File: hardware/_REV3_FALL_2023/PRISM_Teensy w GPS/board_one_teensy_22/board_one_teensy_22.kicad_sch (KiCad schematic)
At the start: 30 parts, among them J1 Micro_SD_Card_Det_Hirose_DM3AT, J3 3387, Q1 AO3400A, Q2 AO3400A, U1 Teensy4.0, U2 GPS-14414, U3 3966, U4 RFM69HCW_Breakout, U5 CT25E-16T150-1, U6 CMI-9605-1280T

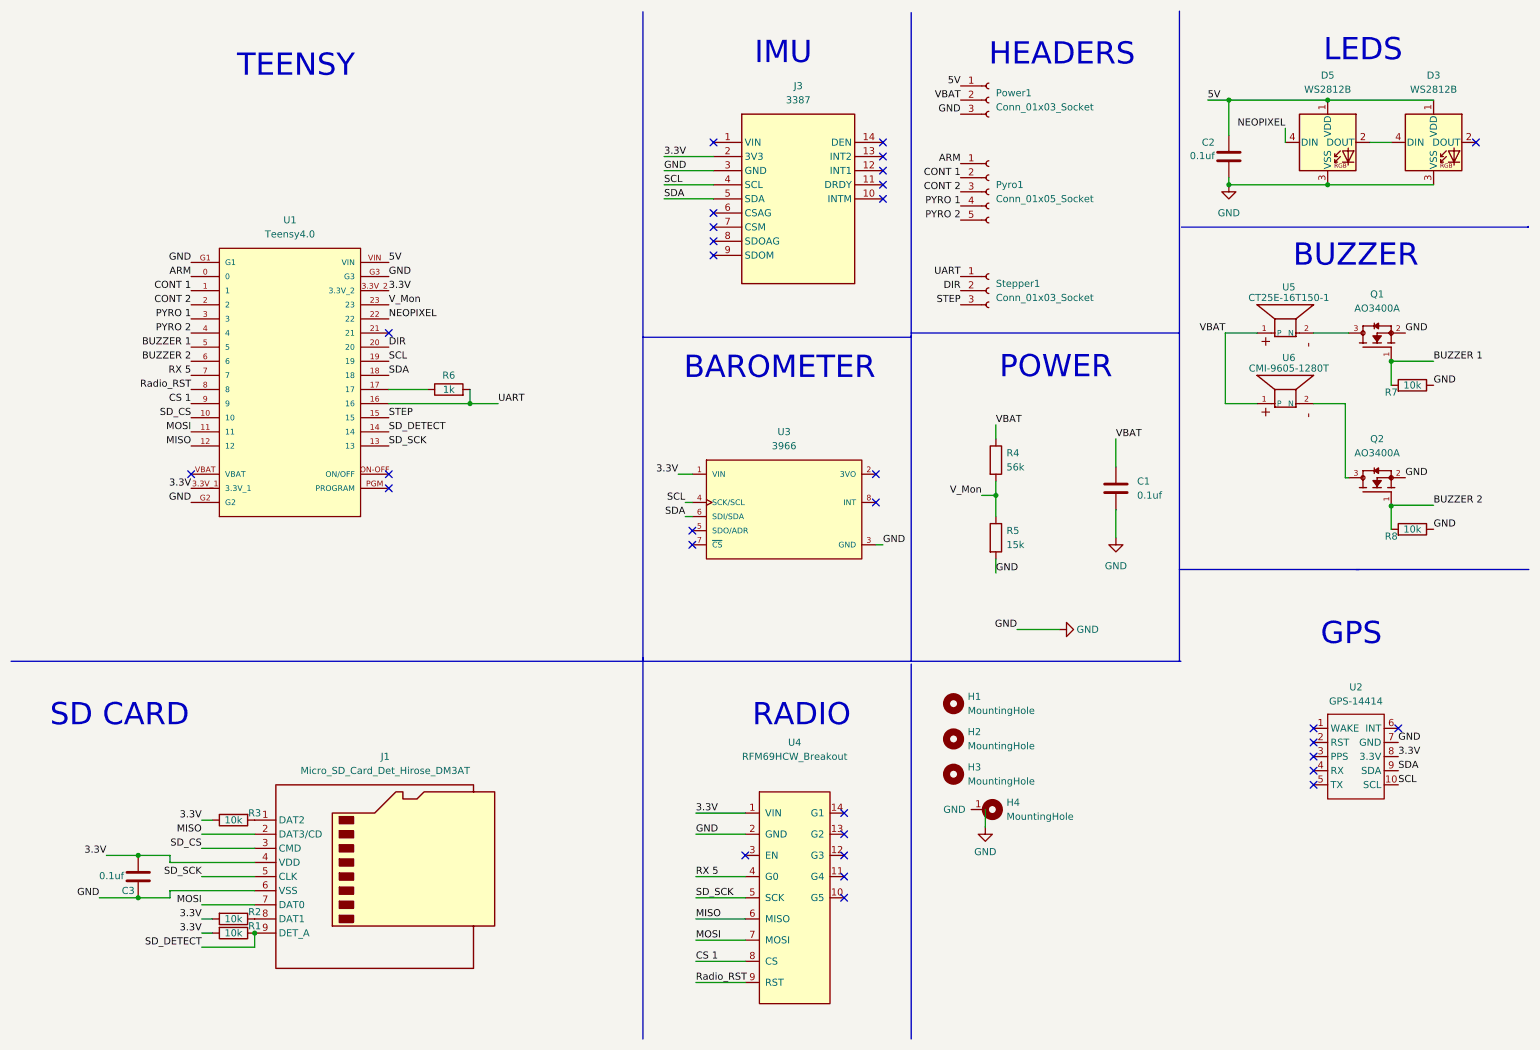
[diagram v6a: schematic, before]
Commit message: Added 3.3V line and fixed analog routing issues on Teensy
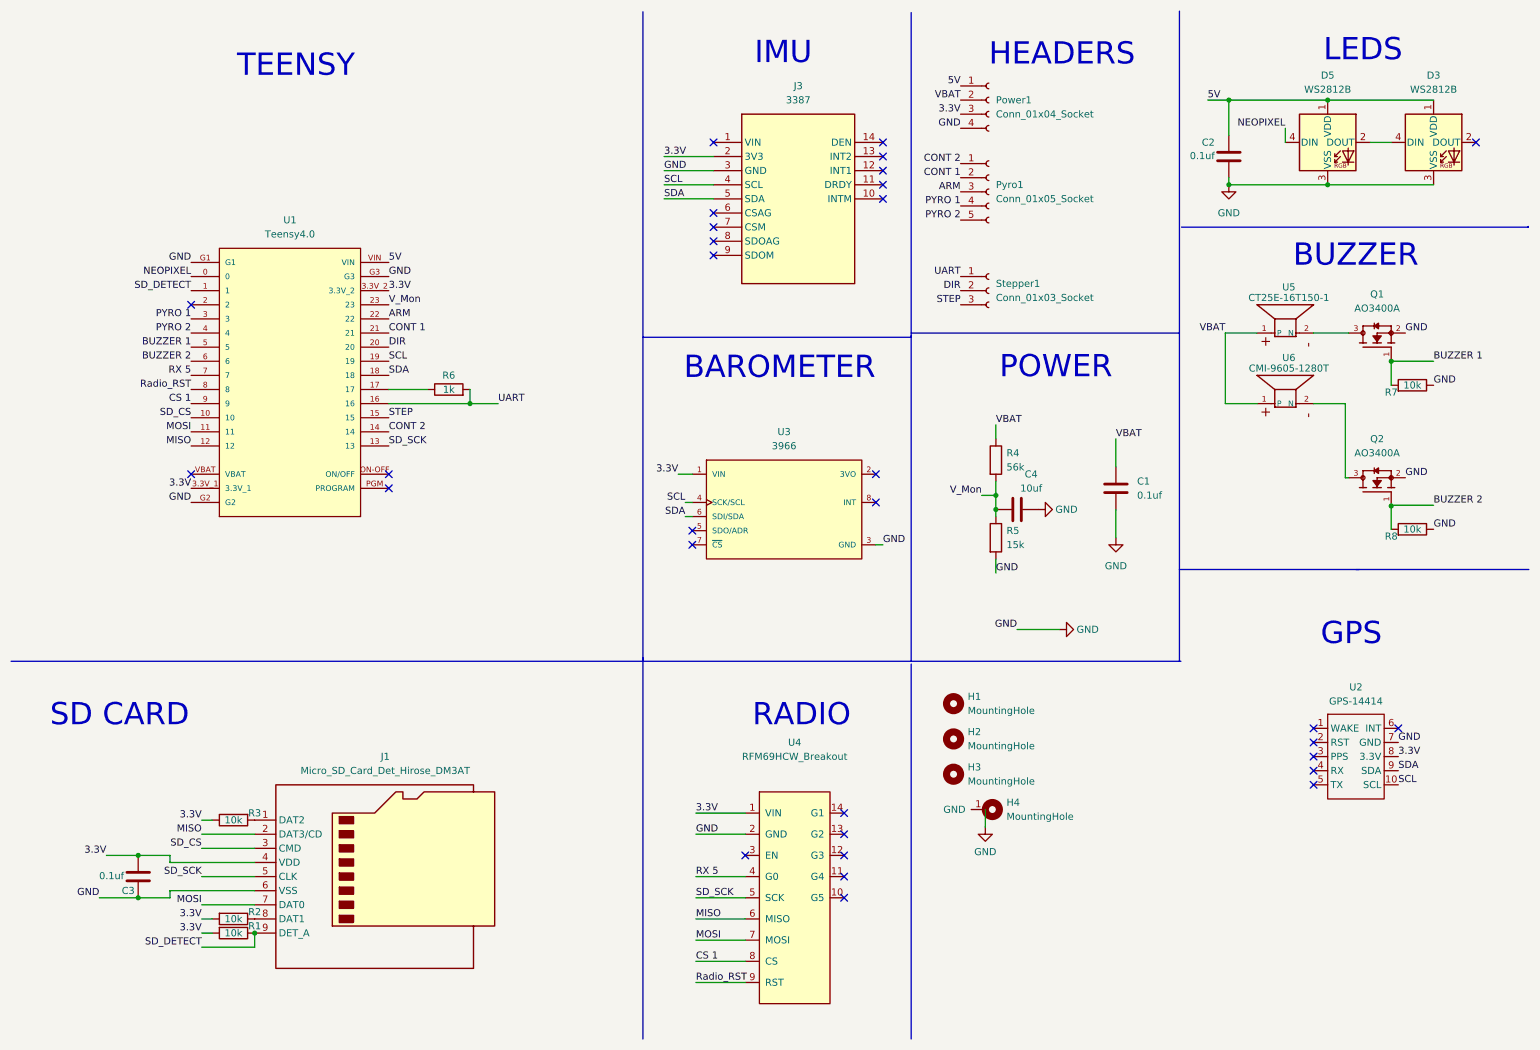
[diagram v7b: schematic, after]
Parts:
- removed Power1: Conn_01x03_Socket, Connector_PinHeader_2.54mm:PinHeader_1x03_P2.54mm_Vertical, symbol Connector:Conn_01x03_Socket
- added C4: 10uf, Capacitor_SMD:C_0603_1608Metric_Pad1.08x0.95mm_HandSolder, symbol Device:C
- added Power1: Conn_01x04_Socket, Connector_PinHeader_2.54mm:PinHeader_1x04_P2.54mm_Vertical, symbol Connector:Conn_01x04_Socket
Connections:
- net 3.3V: now also Power1.3 (Pin_3)
- net 5V: now also Power1.1 (Pin_1)
- net ARM: now also Pyro1.3 (Pin_3), U1.22; no longer Pyro1.1 (Pin_1), U1.0
- net CONT 1: now also U1.21; no longer U1.1
- net CONT 2: now also Pyro1.1 (Pin_1), U1.14; no longer Pyro1.3 (Pin_3), U1.2
- net GND: now also C4.1, Power1.4 (Pin_4)
- net NEOPIXEL: now also U1.0; no longer U1.22
- net SD_DETECT: now also U1.1; no longer U1.14
- net VBAT: now also Power1.2 (Pin_2)
- net V_Mon: now also C4.2
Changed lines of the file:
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@@
   (junction (at 248.92 27.94) (diameter 0) (color 0 0 0 0)
+  )
+  (junction (at 189.23 101.6) (diameter 0) (color 0 0 0 0)
   )
   (junction (at 260.35 74.93) (diameter 0) (color 0 0 0 0)
@@
   (no_connect (at 161.925 167.64))
   (no_connect (at 275.59 35.56))
+  (no_connect (at 44.45 64.77))
   (no_connect (at 44.45 95.25))
   (no_connect (at 246.38 151.13))
   (no_connect (at 246.38 140.97))
   (no_connect (at 161.925 156.21))
-  (no_connect (at 80.01 69.85))
   (no_connect (at 161.925 160.02))
   (no_connect (at 167.64 95.25))
@@
     (stroke (width 0) (type default))
   )
+  (wire (pts (xy 189.23 101.6) (xy 189.23 102.87))
+    (stroke (width 0) (type default))
+  )
   (wire (pts (xy 210.82 88.9) (xy 210.82 93.98))
     (stroke (width 0) (type default))
@@
     (stroke (width 0) (type default))
   )
-  (wire (pts (xy 189.23 99.06) (xy 189.23 102.87))
+  (wire (pts (xy 189.23 99.06) (xy 189.23 101.6))
     (stroke (width 0) (type default))
   )
@@
     (effects (font (size 1.27 1.27)) (justify left bottom))
   )
+  (label "3.3V" (at 182.88 30.48 180) (fields_autoplaced)
+    (effects (font (size 1.27 1.27)) (justify right bottom))
+  )
   (label "SCL" (at 80.01 74.93 0) (fields_autoplaced)
     (effects (font (size 1.27 1.27)) (justify left bottom))
@@
     (effects (font (size 1.27 1.27)) (justify right bottom))
   )
-  (label "SD_DETECT" (at 80.01 87.63 0) (fields_autoplaced)
-    (effects (font (size 1.27 1.27)) (justify left bottom))
-  )
-  (label "ARM" (at 44.45 59.69 180) (fields_autoplaced)
-    (effects (font (size 1.27 1.27)) (justify right bottom))
+  (label "SD_DETECT" (at 44.45 62.23 180) (fields_autoplaced)
+    (effects (font (size 1.27 1.27)) (justify right bottom))
+  )
+  (label "ARM" (at 80.01 67.31 0) (fields_autoplaced)
+    (effects (font (size 1.27 1.27)) (justify left bottom))
   )
   (label "3.3V" (at 46.355 175.26 180) (fields_autoplaced)
@@
     (effects (font (size 1.27 1.27)) (justify right bottom))
   )
-  (label "GND" (at 182.88 30.48 180) (fields_autoplaced)
+  (label "GND" (at 182.88 33.02 180) (fields_autoplaced)
     (effects (font (size 1.27 1.27)) (justify right bottom))
   )
@@
     (effects (font (size 1.27 1.27)) (justify right bottom))
   )
-  (label "CONT 2" (at 44.45 64.77 180) (fields_autoplaced)
-    (effects (font (size 1.27 1.27)) (justify right bottom))
+  (label "CONT 2" (at 80.01 87.63 0) (fields_autoplaced)
+    (effects (font (size 1.27 1.27)) (justify left bottom))
   )
   (label "MISO" (at 135.255 175.26 0) (fields_autoplaced)
@@
     (effects (font (size 1.27 1.27)) (justify left bottom))
   )
-  (label "CONT 2" (at 182.88 44.45 180) (fields_autoplaced)
+  (label "CONT 2" (at 182.88 39.37 180) (fields_autoplaced)
     (effects (font (size 1.27 1.27)) (justify right bottom))
   )
@@
     (effects (font (size 1.27 1.27)) (justify right bottom))
   )
-  (label "ARM" (at 182.88 39.37 180) (fields_autoplaced)
+  (label "ARM" (at 182.88 44.45 180) (fields_autoplaced)
     (effects (font (size 1.27 1.27)) (justify right bottom))
   )
@@
     (effects (font (size 1.27 1.27)) (justify left bottom))
   )
-  (label "CONT 1" (at 44.45 62.23 180) (fields_autoplaced)
-    (effects (font (size 1.27 1.27)) (justify right bottom))
+  (label "CONT 1" (at 80.01 69.85 0) (fields_autoplaced)
+    (effects (font (size 1.27 1.27)) (justify left bottom))
   )
   (label "BUZZER 2" (at 267.97 100.838 0) (fields_autoplaced)
@@
     (effects (font (size 1.27 1.27)) (justify left bottom))
   )
-  (label "NEOPIXEL" (at 80.01 67.31 0) (fields_autoplaced)
-    (effects (font (size 1.27 1.27)) (justify left bottom))
+  (label "NEOPIXEL" (at 44.45 59.69 180) (fields_autoplaced)
+    (effects (font (size 1.27 1.27)) (justify right bottom))
   )
   (label "PYRO 1" (at 182.88 46.99 180) (fields_autoplaced)
@@
   (label "5V" (at 182.88 25.4 180) (fields_autoplaced)
     (effects (font (size 1.27 1.27)) (justify right bottom))
-  )
-  (symbol (lib_id "Connector:Conn_01x03_Socket") (at 187.96 27.94 0) (unit 1)
-    (in_bom yes) (on_board yes) (dnp no) (fields_autoplaced)
-    (property "Reference" "Power1" (at 189.23 26.67 0)
-      (effects (font (size 1.27 1.27)) (justify left))
-    )
-    (property "Value" "Conn_01x03_Socket" (at 189.23 29.21 0)
-      (effects (font (size 1.27 1.27)) (justify left))
-    )
-    (property "Footprint" "Connector_PinHeader_2.54mm:PinHeader_1x03_P2.54mm_Vertical" (at 187.96 27.94 0)
-      (effects (font (size 1.27 1.27)) hide)
-    )
-    (property "Datasheet" "~" (at 187.96 27.94 0)
-      (effects (font (size 1.27 1.27)) hide)
-    )
-    (pin "1")
-    (pin "2")
-    (pin "3")
-    (instances
-      (project "board_one_teensy_22"
-        (path "/7a48c3b0-2761-409e-ae2f-7ebae3820225"
-          (reference "Power1") (unit 1)
-        )
-      )
-    )
   )
   (symbol (lib_id "LED:WS2812B") (at 248.92 35.56 0) (unit 1)
@@
     )
   )
+  (symbol (lib_name "GND_1") (lib_id "power:GND") (at 196.85 101.6 90) (unit 1)
+    (in_bom yes) (on_board yes) (dnp no)
+    (property "Reference" "#PWR05" (at 203.2 101.6 0)
+      (effects (font (size 1.27 1.27)) hide)
+    )
+    (property "Value" "GND" (at 201.93 101.6 90)
+      (effects (font (size 1.27 1.27)))
+    )
+    (property "Footprint" "" (at 196.85 101.6 0)
+      (effects (font (size 1.27 1.27)) hide)
+    )
+    (property "Datasheet" "" (at 196.85 101.6 0)
+      (effects (font (size 1.27 1.27)) hide)
+    )
+    (pin "1")
+    (instances
+      (project "board_one_teensy_22"
+        (path "/7a48c3b0-2761-409e-ae2f-7ebae3820225"
+          (reference "#PWR05") (unit 1)
+        )
+      )
+    )
+  )
   (symbol (lib_id "GPS:GPS-14414") (at 254 142.24 0) (unit 1)
     (in_bom yes) (on_board yes) (dnp no) (fields_autoplaced)
@@
     )
   )
+  (symbol (lib_id "Connector:Conn_01x04_Socket") (at 187.96 27.94 0) (unit 1)
+    (in_bom yes) (on_board yes) (dnp no) (fields_autoplaced)
+    (property "Reference" "Power1" (at 189.23 27.94 0)
+      (effects (font (size 1.27 1.27)) (justify left))
+    )
+    (property "Value" "Conn_01x04_Socket" (at 189.23 30.48 0)
+      (effects (font (size 1.27 1.27)) (justify left))
+    )
+    (property "Footprint" "Connector_PinHeader_2.54mm:PinHeader_1x04_P2.54mm_Vertical" (at 187.96 27.94 0)
+      (effects (font (size 1.27 1.27)) hide)
+    )
+    (property "Datasheet" "~" (at 187.96 27.94 0)
+      (effects (font (size 1.27 1.27)) hide)
+    )
+    (pin "2")
+    (pin "1")
+    (pin "3")
+    (pin "4")
+    (instances
+      (project "board_one_teensy_22"
+        (path "/7a48c3b0-2761-409e-ae2f-7ebae3820225"
+          (reference "Power1") (unit 1)
+        )
+      )
+    )
+  )
   (symbol (lib_id "AO3400A:AO3400A") (at 257.81 98.425 90) (unit 1)
     (in_bom yes) (on_board yes) (dnp no) (fields_autoplaced)
@@
         )
       )
+    )
+  )
+  (symbol (lib_id "Device:C") (at 193.04 101.6 270) (unit 1)
+    (in_bom yes) (on_board yes) (dnp no)
+    (property "Reference" "C4" (at 195.58 95.25 90)
+      (effects (font (size 1.27 1.27)))
+    )
+    (property "Value" "10uf" (at 195.58 97.79 90)
+      (effects (font (size 1.27 1.27)))
+    )
+    (property "Footprint" "Capacitor_SMD:C_0603_1608Metric_Pad1.08x0.95mm_HandSolder" (at 189.23 102.5652 0)
+      (effects (font (size 1.27 1.27)) hide)
+    )
+    (property "Datasheet" "~" (at 193.04 101.6 0)
+      (effects (font (size 1.27 1.27)) hide)
+    )
+    (property "Vendor" "C19702" (at 193.04 101.6 0)
+      (effects (font (size 1.27 1.27)) hide)
+    )
+    (pin "1")
+    (pin "2")
+    (instances
+      (project "board_one_teensy_22"
+        (path "/7a48c3b0-2761-409e-ae2f-7ebae3820225"
+          (reference "C4") (unit 1)
+        )
+      )

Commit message: Forgot to save schematic from last push
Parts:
- C4: footprint Capacitor_SMD:C_0603_1608Metric_Pad1.08x0.95mm_HandSolder -> Capacitor_SMD:C_0603_1608Metric
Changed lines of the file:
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@@
       (effects (font (size 1.27 1.27)))
     )
-    (property "Footprint" "Capacitor_SMD:C_0603_1608Metric_Pad1.08x0.95mm_HandSolder" (at 189.23 102.5652 0)
+    (property "Footprint" "Capacitor_SMD:C_0603_1608Metric" (at 189.23 102.5652 0)
       (effects (font (size 1.27 1.27)) hide)
     )
